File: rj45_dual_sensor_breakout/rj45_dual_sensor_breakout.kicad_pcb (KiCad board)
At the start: 2 copper layers, 30.5 x 48.9 mm, 9 parts, among them J1 RJ45, J2 GND, J3 V, J4 GPIO, J5 RJ45

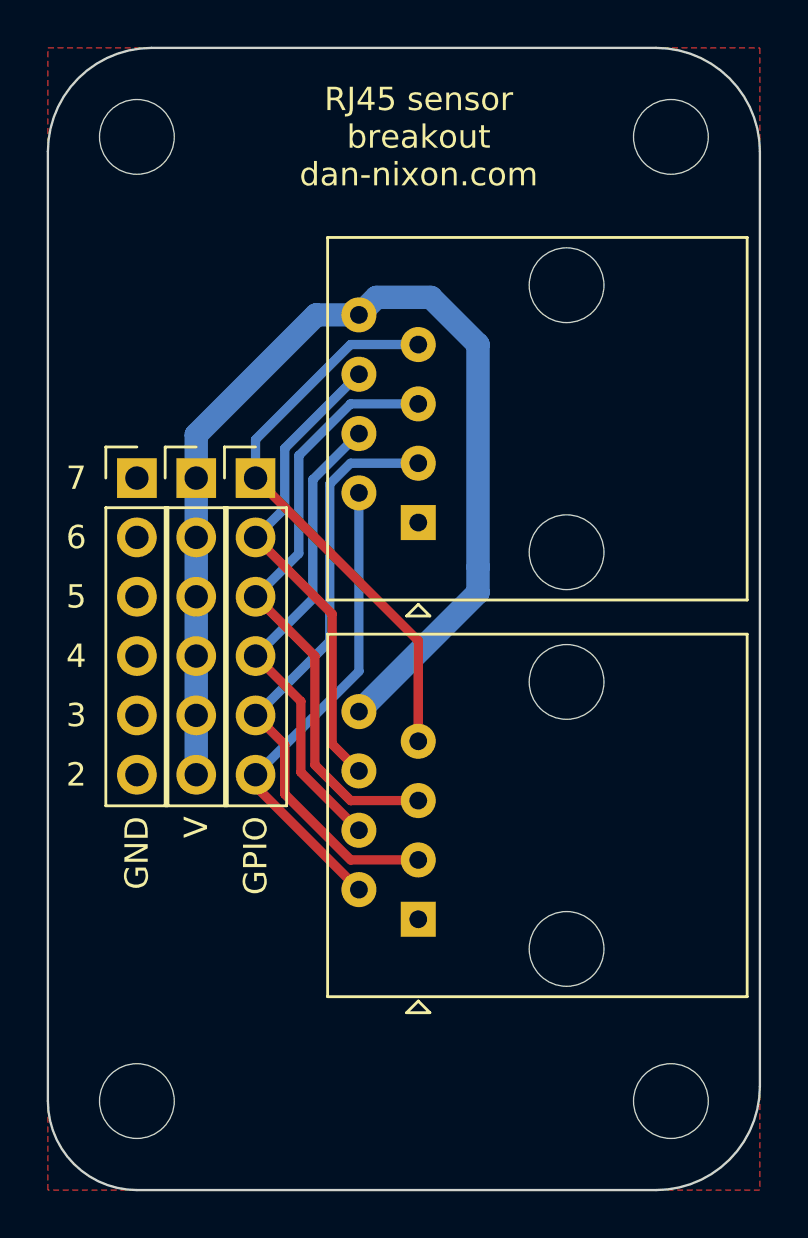
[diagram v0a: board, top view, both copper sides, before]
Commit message: RJ45 dual sensor breakout
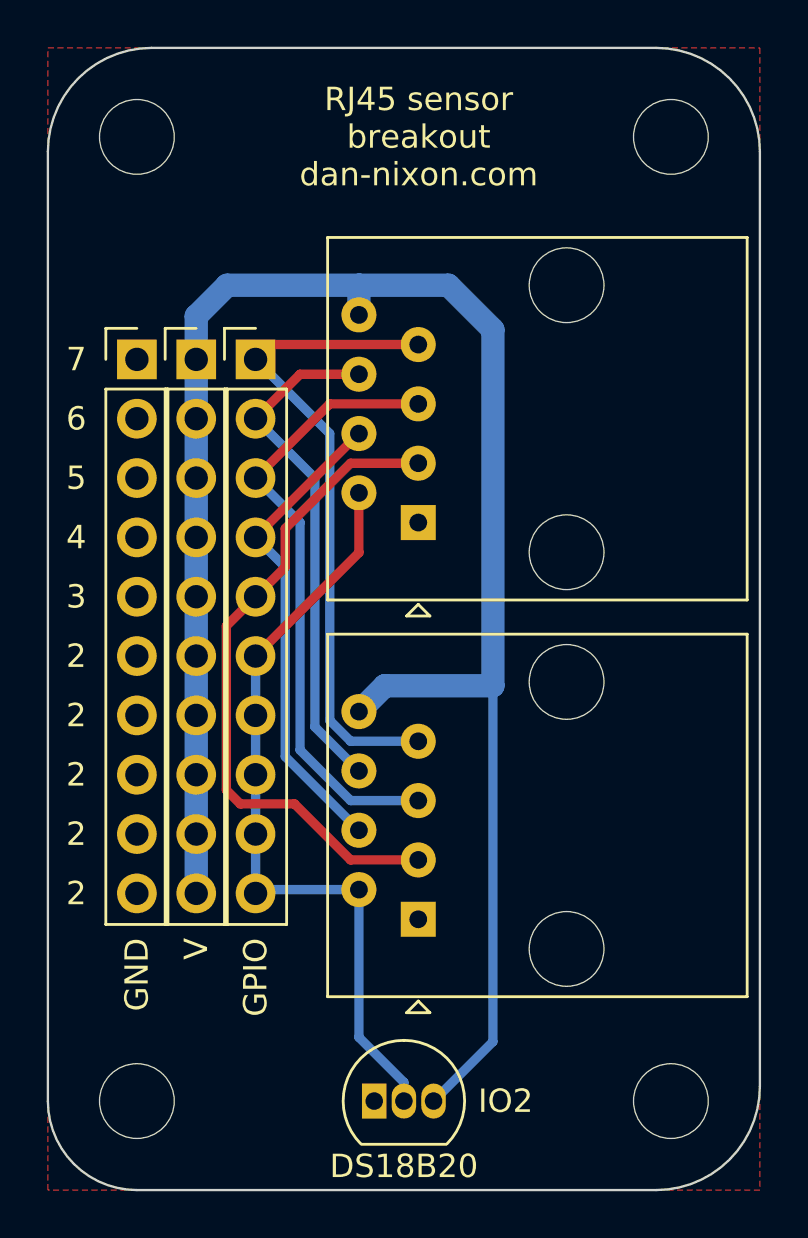
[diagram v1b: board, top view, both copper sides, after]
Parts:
- added U1: DS18B20, Package_TO_SOT_THT:TO-92_Inline, F.Cu at (102.2, 95.2)
- J2, J3, J4: footprint Connector_PinHeader_2.54mm:PinHeader_1x06_P2.54mm_Vertical -> Connector_PinHeader_2.54mm:PinHeader_1x10_P2.54mm_Vertical
- moved J2 5.08 mm to (92.1, 63.5)
- moved J3 5.08 mm to (94.6, 63.5)
- moved J4 5.08 mm to (97.2, 63.5)
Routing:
- net VBUS: track 47.7 -> 80.3 mm
- net /P2: track 20.6 -> 33.3 mm
- net /P7: track 24.4 -> 28.2 mm
- net /P3: track 26.1 -> 28.5 mm
- net /P6: track 20.6 -> 22.1 mm
- net /P5: track 26.1 -> 26.7 mm
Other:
- board text added: "IO2"
